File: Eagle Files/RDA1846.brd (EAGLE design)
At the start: 69.4 x 26.1 mm, 42 parts, among them X1 SMA-142-0701-871/876, X2 SMA-142-0701-871/876

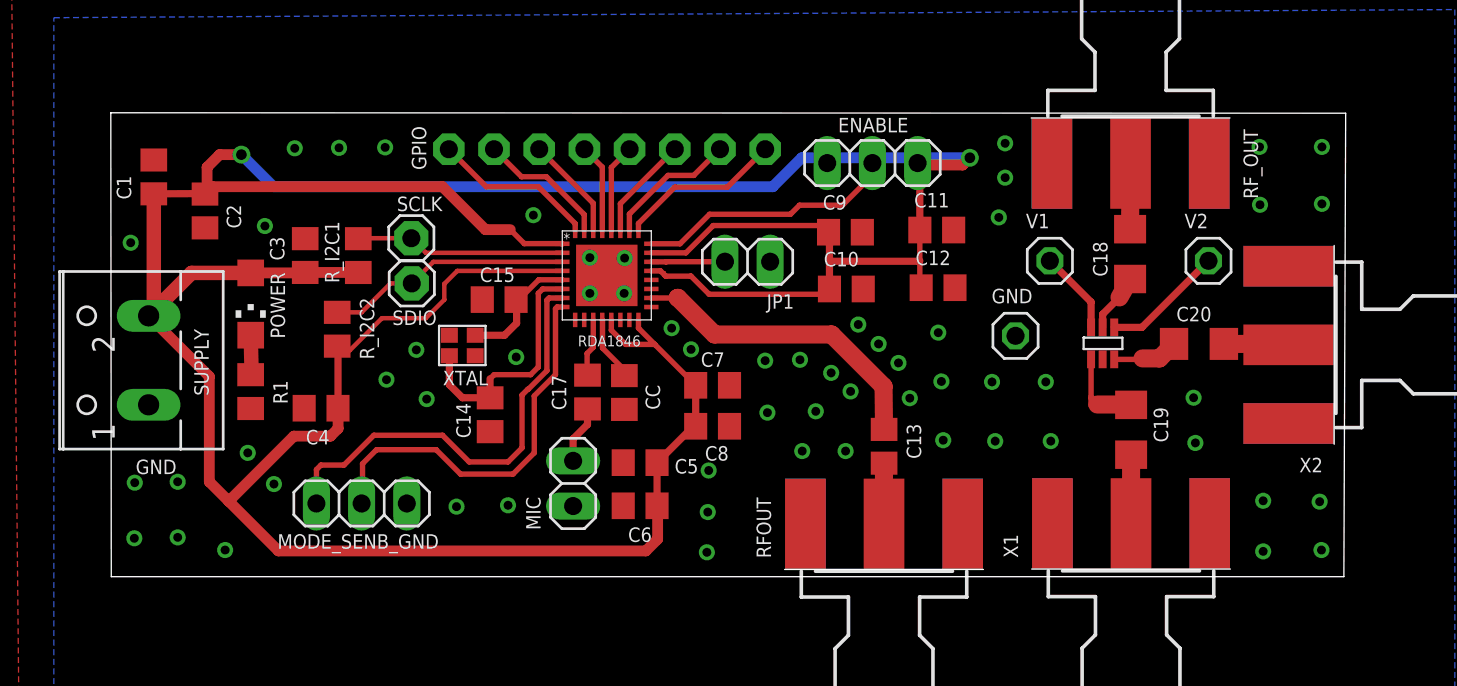
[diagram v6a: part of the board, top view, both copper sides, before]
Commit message: Added mounting holes and values of resisters and capacitors
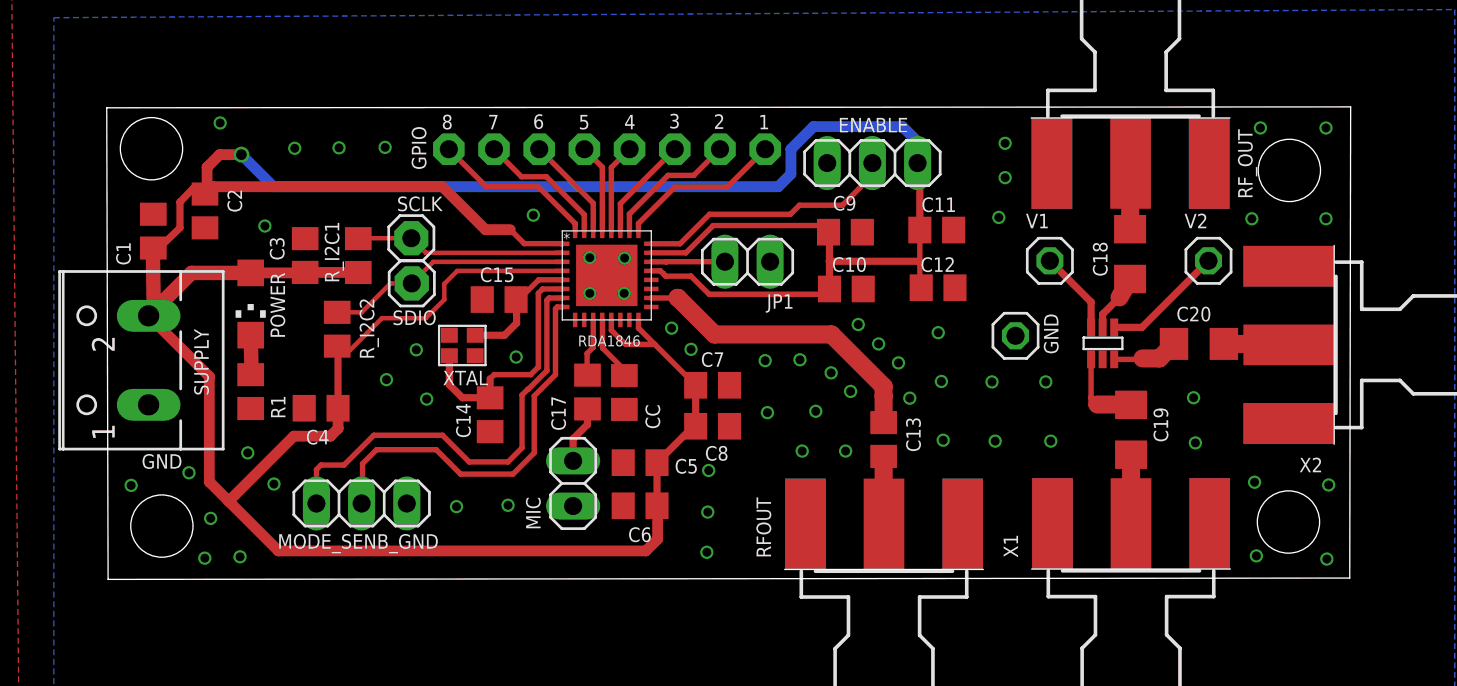
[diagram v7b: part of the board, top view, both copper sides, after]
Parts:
- moved C1 3.05 mm to (2.37, 25.2)
- moved C13 0.38 mm to (43.4, 13.5)
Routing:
- net VDD: track 253.6 -> 271.6 mm, vias 2 -> 1
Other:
- board size 69.4 x 26.1 mm -> 69.9 x 26.6 mm
- board text added: "1"
- board text added: "2"
- board text added: "3"
- board text added: "4"
- board text added: "5"
- board text added: "6"
- board text added: "7"
- board text added: "8"
